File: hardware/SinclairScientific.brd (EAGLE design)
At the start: 47 x 108 mm, 117 parts, among them J1 JSTPH, J3 USB-MICRO, U2 SPX3819-3.3, U3 MCP73831T-2ACI/OT, U4 ATSAMD21G18, U5 W25Q128JVWSON_6X5, X2 32.768

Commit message: Changed button spacing, finalized rev 1C layouts
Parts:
- moved U$50 10.0 mm to (12.6, 49.8)
- moved U$52 10.0 mm to (34.4, 17.5)
- moved U$53 10.0 mm to (34.4, 49.8)
- moved U$51 9.91 mm to (12.4, 17.5)
- moved D1 1.27 mm to (33.3, 57.1)
- moved S1 1.14 mm to (39.9, 56.2)
- moved SW-1 1.14 mm to (7.11, 22.9)
- moved SW-4 1.14 mm to (7.11, 33.7)
- moved SW-7 1.14 mm to (7.11, 44.5)
- moved SW-DIV 1.14 mm to (39.9, 33.7)
- moved SW-DWN 1.14 mm to (7.11, 12.1)
- moved SW-MINUS 1.14 mm to (39.9, 12.1)
- moved SW-MULT 1.14 mm to (39.9, 44.5)
- moved SW-PLUS 1.14 mm to (39.9, 22.9)
- moved SW-UP 1.14 mm to (7.11, 55.2)
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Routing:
- net D9/A7: track 138.8 -> 147.5 mm
- net D16/A2: track 152.3 -> 157.7 mm
- net D15/A1: track 146.0 -> 150.9 mm
- net D11: track 135.2 -> 138.5 mm
- net VBUS: track 115.2 -> 118.1 mm
- net D8/A6: track 169.2 -> 171.7 mm
- net D12: track 185.2 -> 187.7 mm
- net N$3: track 75.9 -> 77.5 mm
- net VBAT: track 26.3 -> 24.9 mm
- net D4: track 118.9 -> 120.3 mm
- net D17/A3: track 111.7 -> 112.9 mm
- net VBUS_SW: track 28.0 -> 27.2 mm
- net D7: track 137.8 -> 138.5 mm
- net GND: vias 82 -> 96

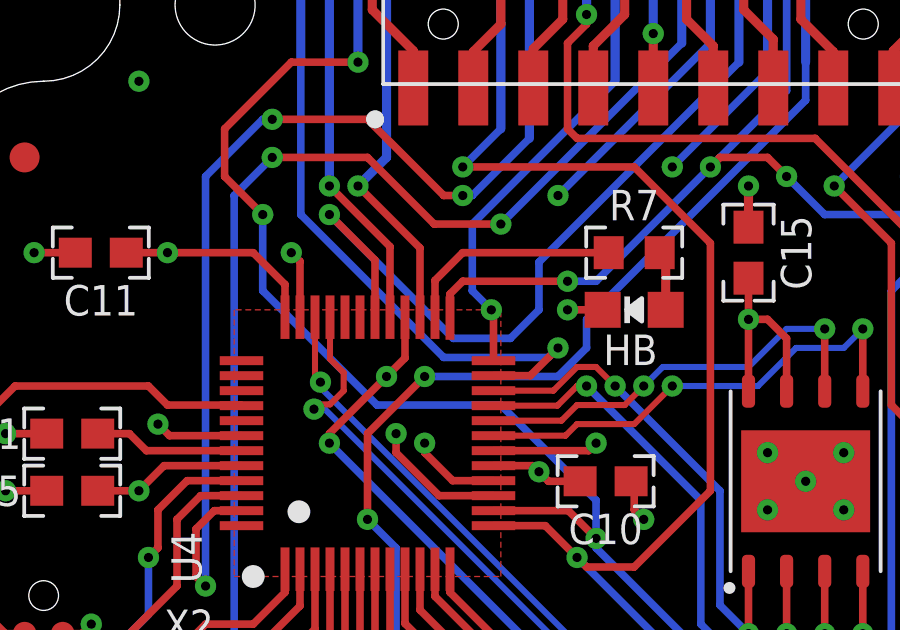
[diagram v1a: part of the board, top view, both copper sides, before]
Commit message: Updated BOM and added BOM attributes to schematic
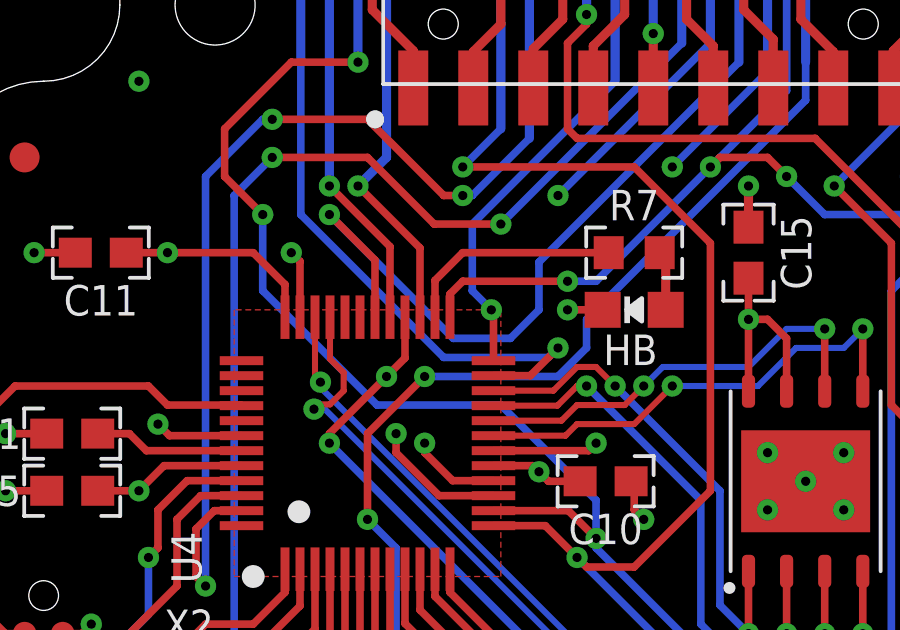
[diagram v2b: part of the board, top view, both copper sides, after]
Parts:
- C1, C12, C14, C7: value 1uF -> 1u
- C13, C3, C6, C8: value 10uF -> 10u
- C15, C5: value 100nF -> 100n
- C2, C4: value 22pF -> 22p
- CHG: value RED -> GREEN-RA
- HB, L1: value RED -> GREEN
- J2: value (none) -> 87759-1850
- SW-0, SW-1, SW-2, SW-3, SW-4, SW-5, SW-6, SW-7, SW-8, SW-9, SW-C, SW-DIV, SW-DWN, SW-E, SW-MINUS, SW-MULT, SW-PLUS, SW-UP: value SPST_TACT-6X6 -> SPST_TACT-TL3301SPF
- SW-0_CAP, SW-1_CAP, SW-2_CAP, SW-3_CAP, SW-4_CAP, SW-5_CAP, SW-6_CAP, SW-7_CAP, SW-8_CAP, SW-9_CAP, SW-C_CAP, SW-DIV_CAP, SW-DWN_CAP, SW-E_CAP, SW-MINUS_CAP, SW-MULT_CAP, SW-PLUS_CAP, SW-UP_CAP: value SW-CAP_1SWXXX -> SW-CAP_1SXXX
- renumbered U$18 to SILK-QC, U$19 to SW-1_CAP, U$2 to FID2, U$20 to SW-7_CAP, U$28 to SW-UP_CAP, U$31 to SW-MULT_CAP, U$32 to SW-2_CAP, U$33 to SW-8_CAP, U$34 to SW-DWN_CAP, U$35 to FID3, U$37 to SW-DIV_CAP, U$40 to SW-3_CAP, U$41 to SW-9_CAP, U$42 to SW-PLUS_CAP, U$43 to SW-MINUS_CAP, U$44 to SW-4_CAP, U$45 to SW-0_CAP, U$46 to SW-E_CAP, U$47 to SW-6_CAP, U$48 to SW-5_CAP, U$49 to SW-C_CAP, U$7 to FID1
